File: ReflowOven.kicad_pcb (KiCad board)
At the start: 4 copper layers, 157.5 x 155.4 mm, 156 parts, among them J201 Conn_02x05_Odd_Even, J501 IEC320-C14, J502 IEC-NEMA-3PIN, J601 Thermocouple_Conn, J701 Conn_01x03_Male, J702 Microfit-4pin, J703 Conn_01x06_Male, J704 USB_C_Receptacle_USB2.0, K501 G5RLU1E, P501 RAC10-3.3SK_277, SW201 B3U-1100P, SW401 SW_Push, SW402 SW_Push, SW403 SW_Push, SW404 RotaryEncoder_Switch, U201 STM32F302C6Tx, U202 NCV7357, U301 PCF5331ATT_AJ, U401 74HC193, U402 TCA9534, U403 74HC193, U404 HEF4013B, U405 SN74LVC2G08, U406 74LVC2G14, U407 74HC86D, U408 HEF4013B, U409 SD-Card-NOSHELL, U501 MAX4684_5, U502 INA226, U601 MCP96RL01T, U701 TPD1E05U06PYR, U702 TPD1E05U06PYR, X201 OSC_4PIN, X401 OSC_4PIN

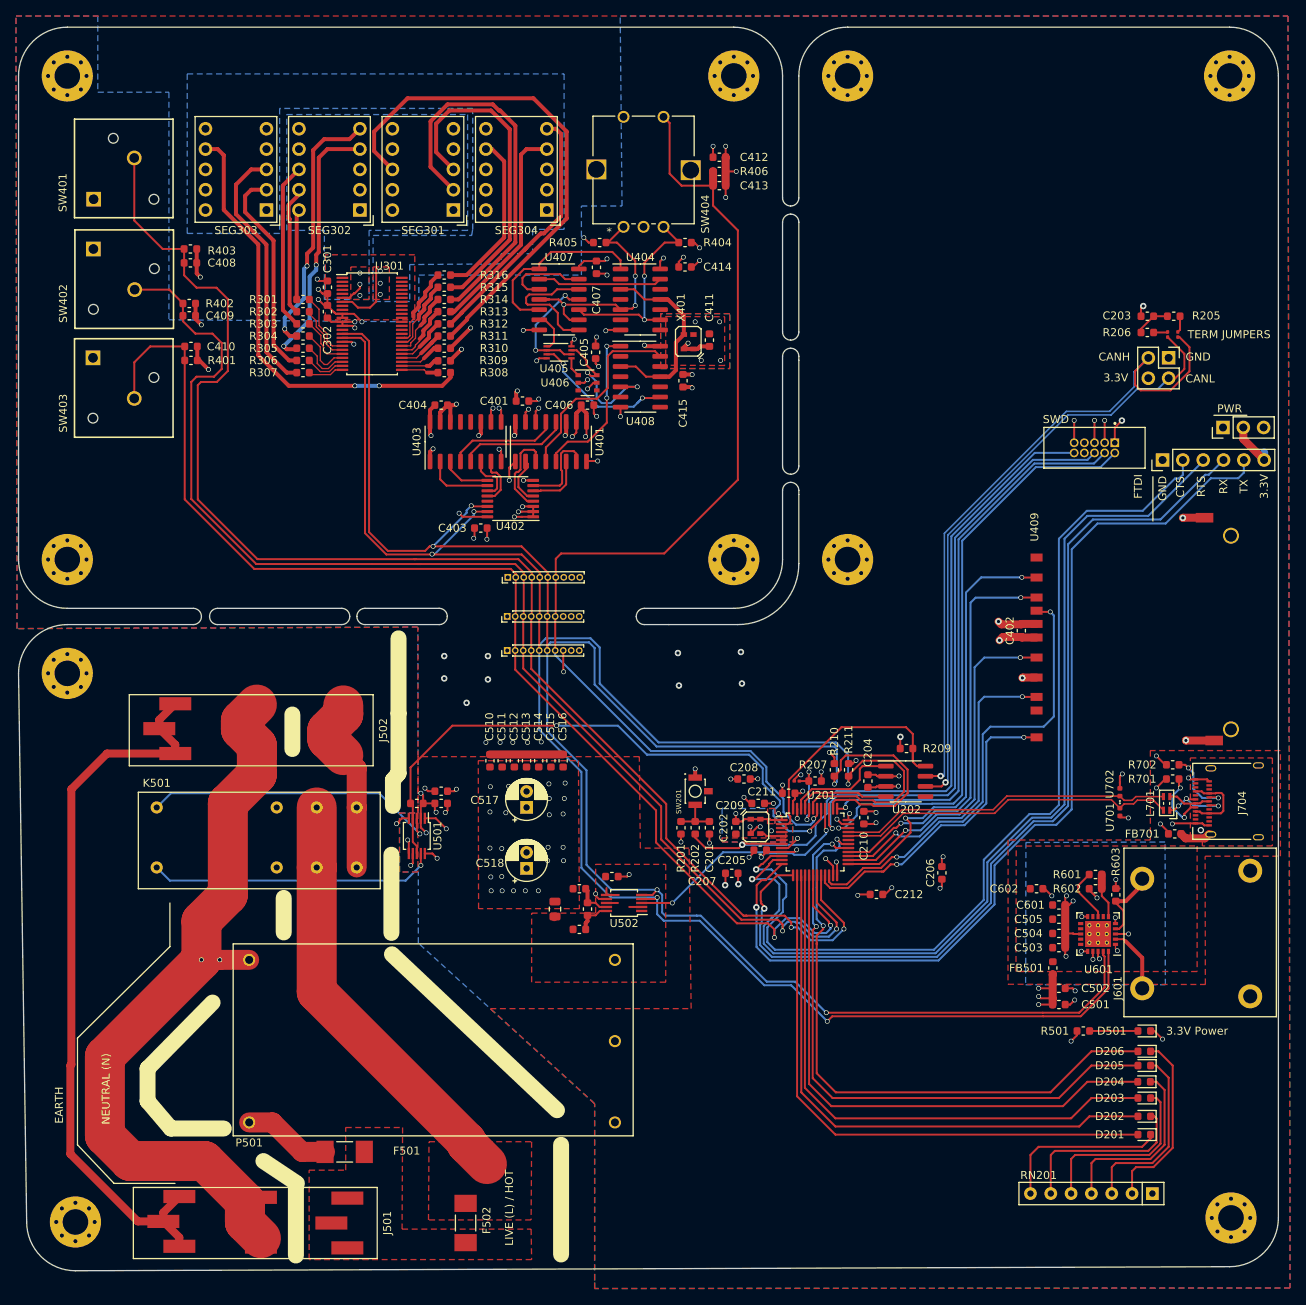
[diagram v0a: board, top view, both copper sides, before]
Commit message: Added 3D model
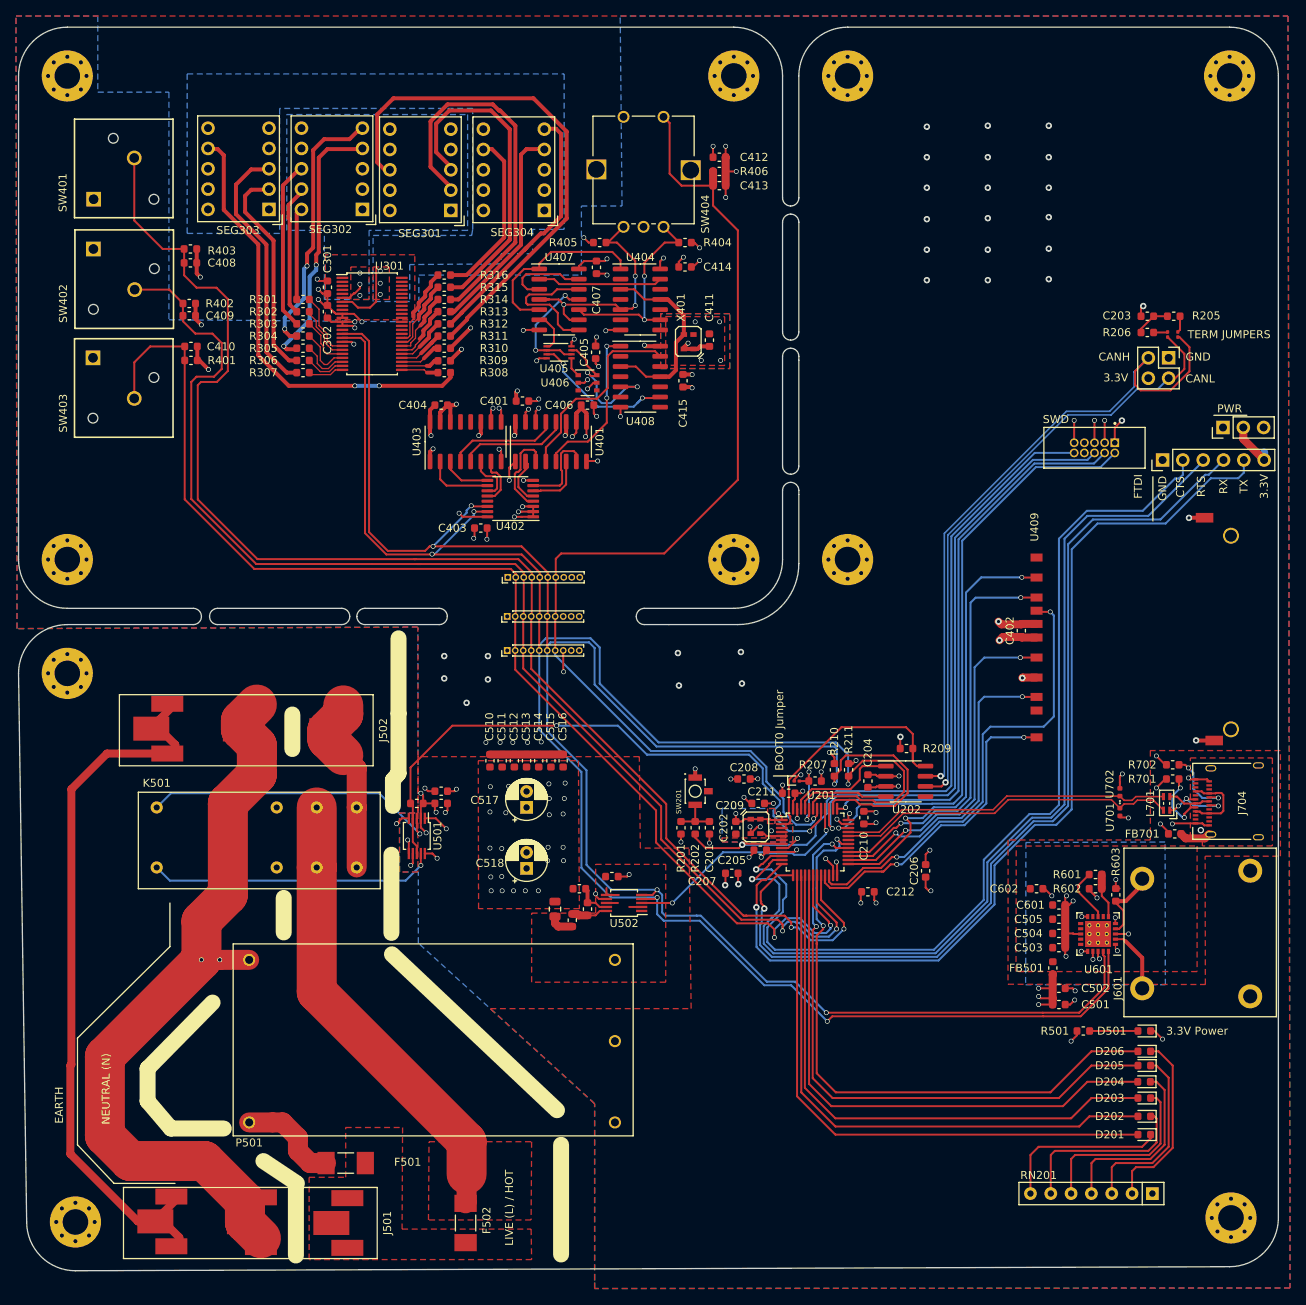
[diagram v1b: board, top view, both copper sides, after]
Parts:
- K501: footprint ReflowOven:G5RLU-1-E DC3 -> ReflowOven:G5RLU-1-EDC3
- SEG301, SEG302, SEG303, SEG304: footprint Display_7Segment:Sx39-1xxxxx -> ReflowOven:7-Segment-CC
- moved SEG301 6.57 mm to (67.3, 43.6)
- moved SEG304 6.57 mm to (79.0, 43.6)
- moved SEG302 6.27 mm to (56.3, 43.4)
- moved SEG303 6.27 mm to (44.6, 43.4)
- moved C206 2.05 mm to (130.7, 131.1)
- moved R503 1.45 mm to (86.5, 137.3), turned to 90 degrees
- moved F501 1.40 mm to (58.2, 167.6)
- moved C212 1.12 mm to (123.4, 133.7)
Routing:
- net Net-(F502-Pad1): track 53.4 -> 57.3 mm
- net /MainsPower/3V3_REG_OUT: track 5.52 -> 8.58 mm
- net Net-(F501-Pad1): track 11.0 -> 12.7 mm
- net /Display/SEG4: track 59.2 -> 60.8 mm
- net /Display/SEG9: track 49.6 -> 51.0 mm
- net GND: track 222.5 -> 221.0 mm, vias 113 -> 122
- net /Display/SEG10: track 86.7 -> 87.7 mm
- net +3V3: track 123.9 -> 124.8 mm, vias 76 -> 85
- net /Display/SEG2: track 58.9 -> 58.4 mm
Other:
- board text added: "BOOT0 Jumper"
